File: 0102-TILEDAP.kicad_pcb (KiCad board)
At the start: 2 copper layers, 42 x 25 mm, 40 parts, among them J1 USB-C, J2 IF, J3 TGT, SW1 SW_Push, U1 SPX3819M5-L-3-3, U2 STM32F103TBUx, Y1 8MHz

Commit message: Update DAPLink to 4-layers
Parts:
- moved D1 0.25 mm to (114.0, 102.5)
- moved D2 0.25 mm to (115.5, 102.5)
- moved D3 0.25 mm to (120.0, 102.5)
- moved J2 0.09 mm to (102.1, 102.5)
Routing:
- net VBUS: track 55.9 -> 38.2 mm, vias 2 -> 1
- net +3V3: track 79.8 -> 76.5 mm
- net GND: track 15.6 -> 13.7 mm, vias 16 -> 98
- added copper zone on In1.Cu, net GND
- added copper zone on In2.Cu, net GND
- added copper zone on In2.Cu, net VBUS
- removed copper zone on B.Cu, net VBUS
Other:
- copper layers 2 -> 4
- board text added: "5"
- board text added: "C"
- board text added: "D"

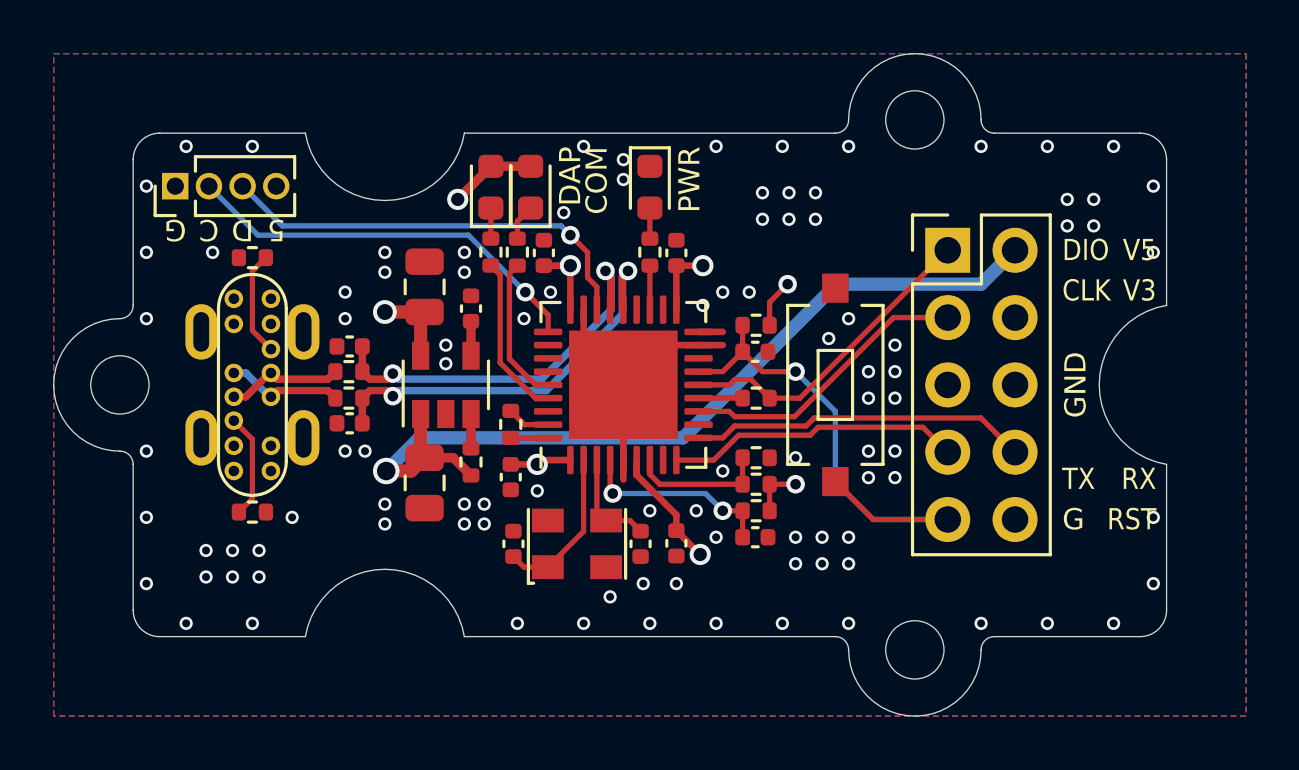
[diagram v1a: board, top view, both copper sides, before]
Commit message: Finish DAPLink with final outline
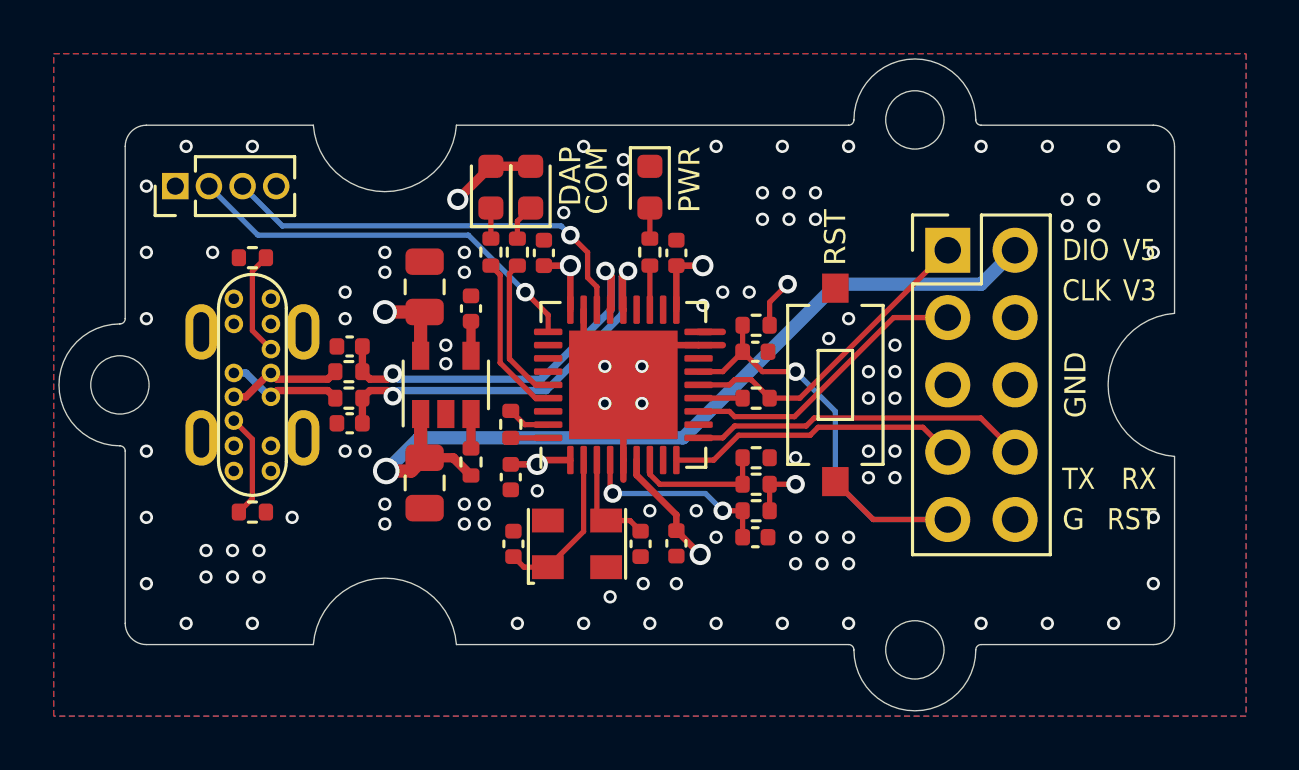
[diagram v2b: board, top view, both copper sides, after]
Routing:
- net GND: vias 98 -> 99
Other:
- board size 42 x 25 mm -> 42.1 x 24.6 mm
- board text added: "#0102 DAPLink V1.0"
- board text added: "5V"
- board text added: "JLCJLCJLCJLC"
- board text added: "SWCK"
- board text added: "SWIO"
- board text removed: "5"
- board text removed: "C"
- board text removed: "D"
